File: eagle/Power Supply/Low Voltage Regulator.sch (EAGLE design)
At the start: 7 parts, among them K1 G5LE, Q1 2N3906

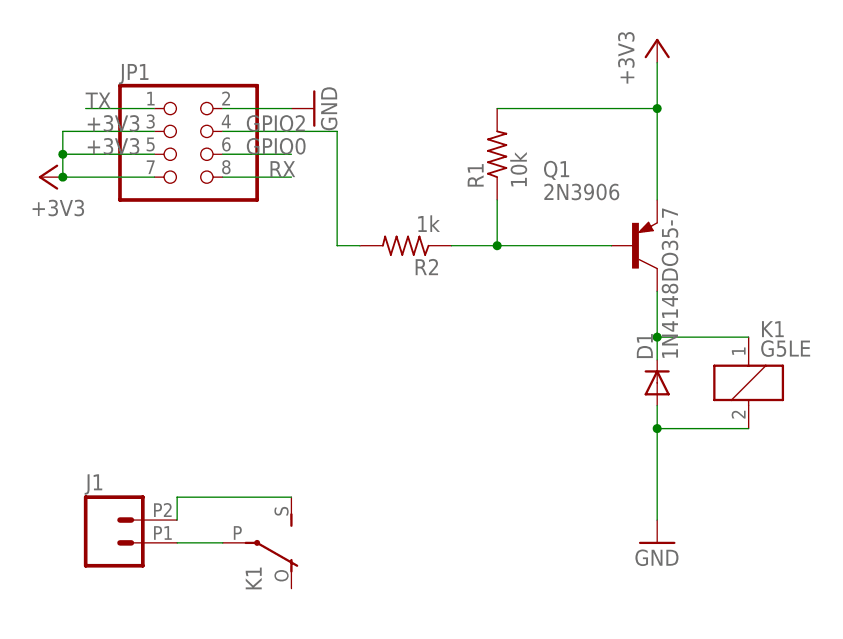
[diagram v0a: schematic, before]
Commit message: Power Supply regulator ref design
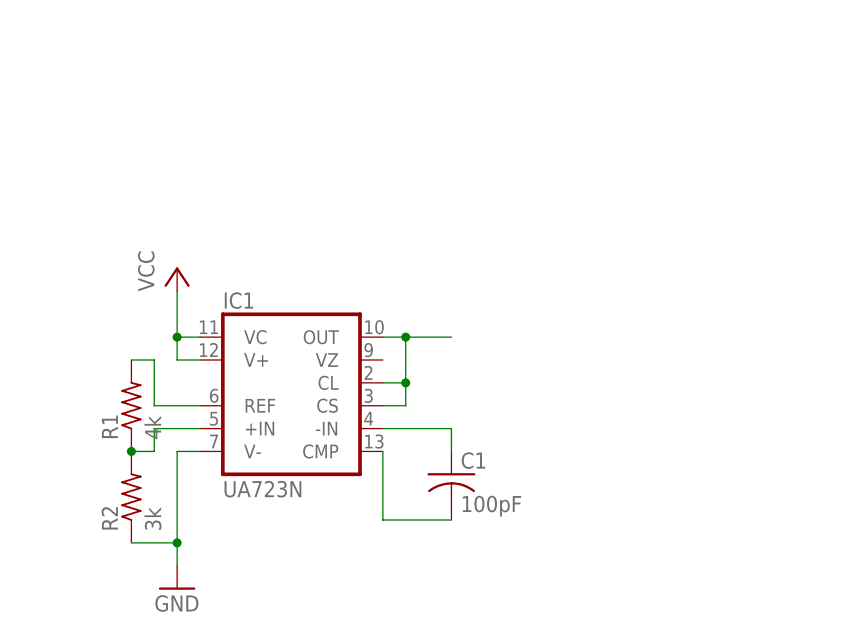
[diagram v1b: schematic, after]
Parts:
- removed D1: 1N4148DO35-7, diode:1N4148DO35-7
- removed J1: (no value), SparkFun-Connectors:M022.54MM_SCREWTERM
- removed JP1: (no value), adafruit:PINHD-2X4
- removed K1: G5LE, relay:G5LE
- removed Q1: 2N3906, transistor-pnp:2N3906
- added C1: 100pF, rcl:C-US050-025X075
- added IC1: UA723N, linear:UA723N
- R1: value 10k -> 4k
- R2: value 1k -> 3k
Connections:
- removed net +3V3: JP1.3, JP1.5, JP1.7, Q1.E, R1.2
- removed net GPIO0: JP1.6
- removed net GPIO2: JP1.4, R2.2
- removed net RX: JP1.8
- removed net TX: JP1.1
- new net N$5: IC1.CL, IC1.CS, IC1.OUT
- new net VCC: IC1.V+, IC1.VC
- net GND: now also IC1.V-, R2.1; no longer D1.A, JP1.2, K11.2
- net N$1: now also IC1.REF, R1.2; no longer Q1.B, R1.1, R2.1
- net N$2: now also IC1.+IN, R1.1, R2.2; no longer D1.C, K11.1, Q1.C
- net N$3: now also C1.1, IC1.-IN; no longer J1.2, K12.S
- net N$4: now also C1.2, IC1.CMP; no longer J1.1, K12.P
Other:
- moved on the sheet: R1, R2
